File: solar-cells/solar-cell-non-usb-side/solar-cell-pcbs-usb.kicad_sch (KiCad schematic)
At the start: 13 parts, among them J1 Solar Cell

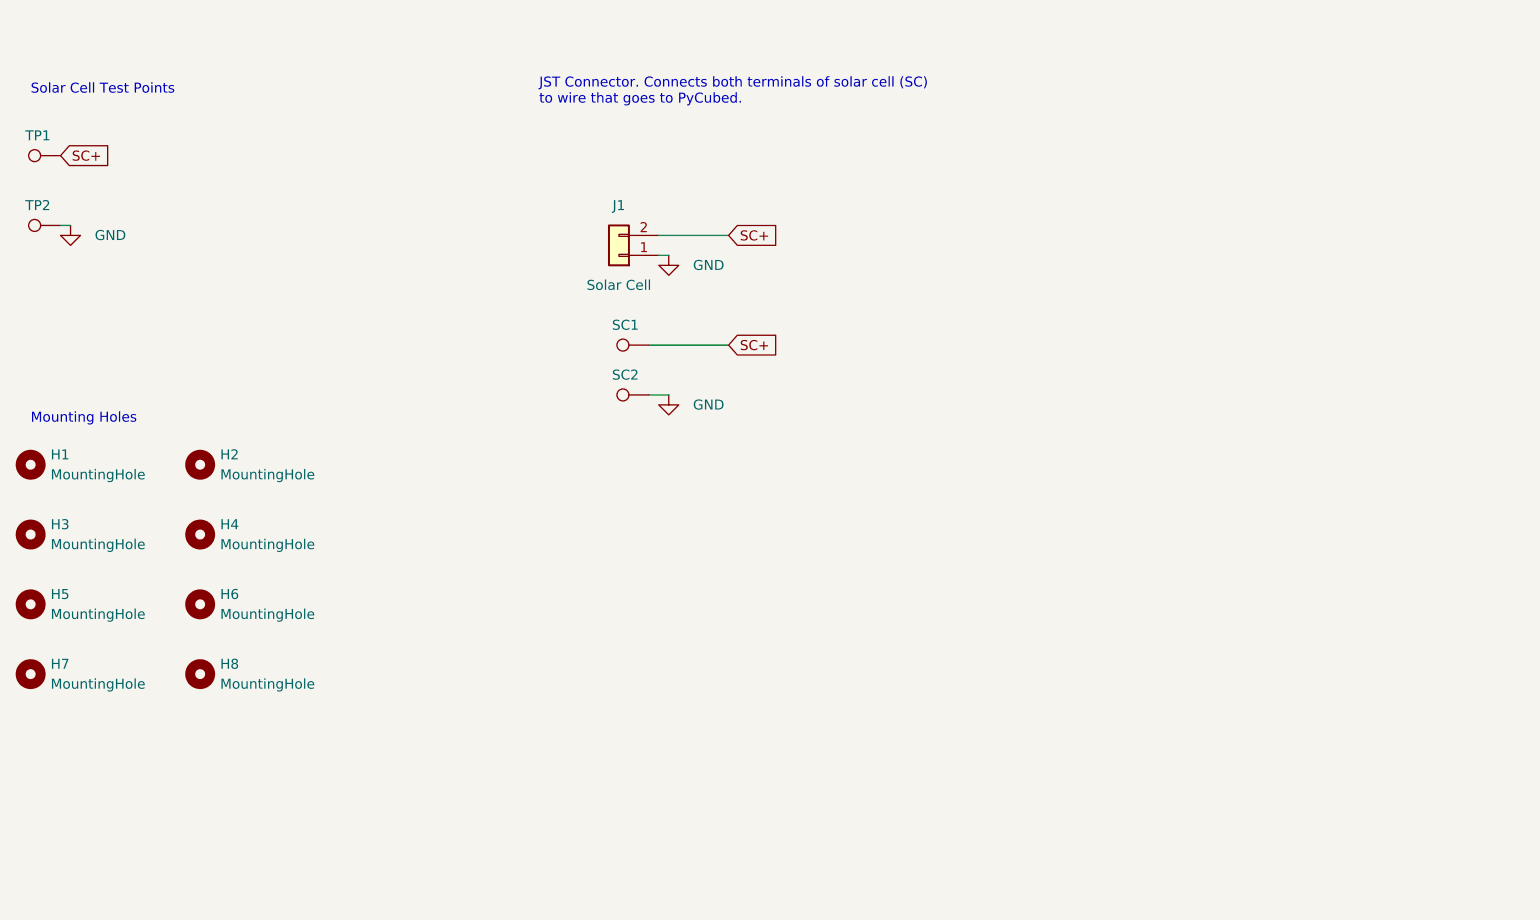
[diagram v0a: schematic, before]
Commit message: updated schematic for new solar cells
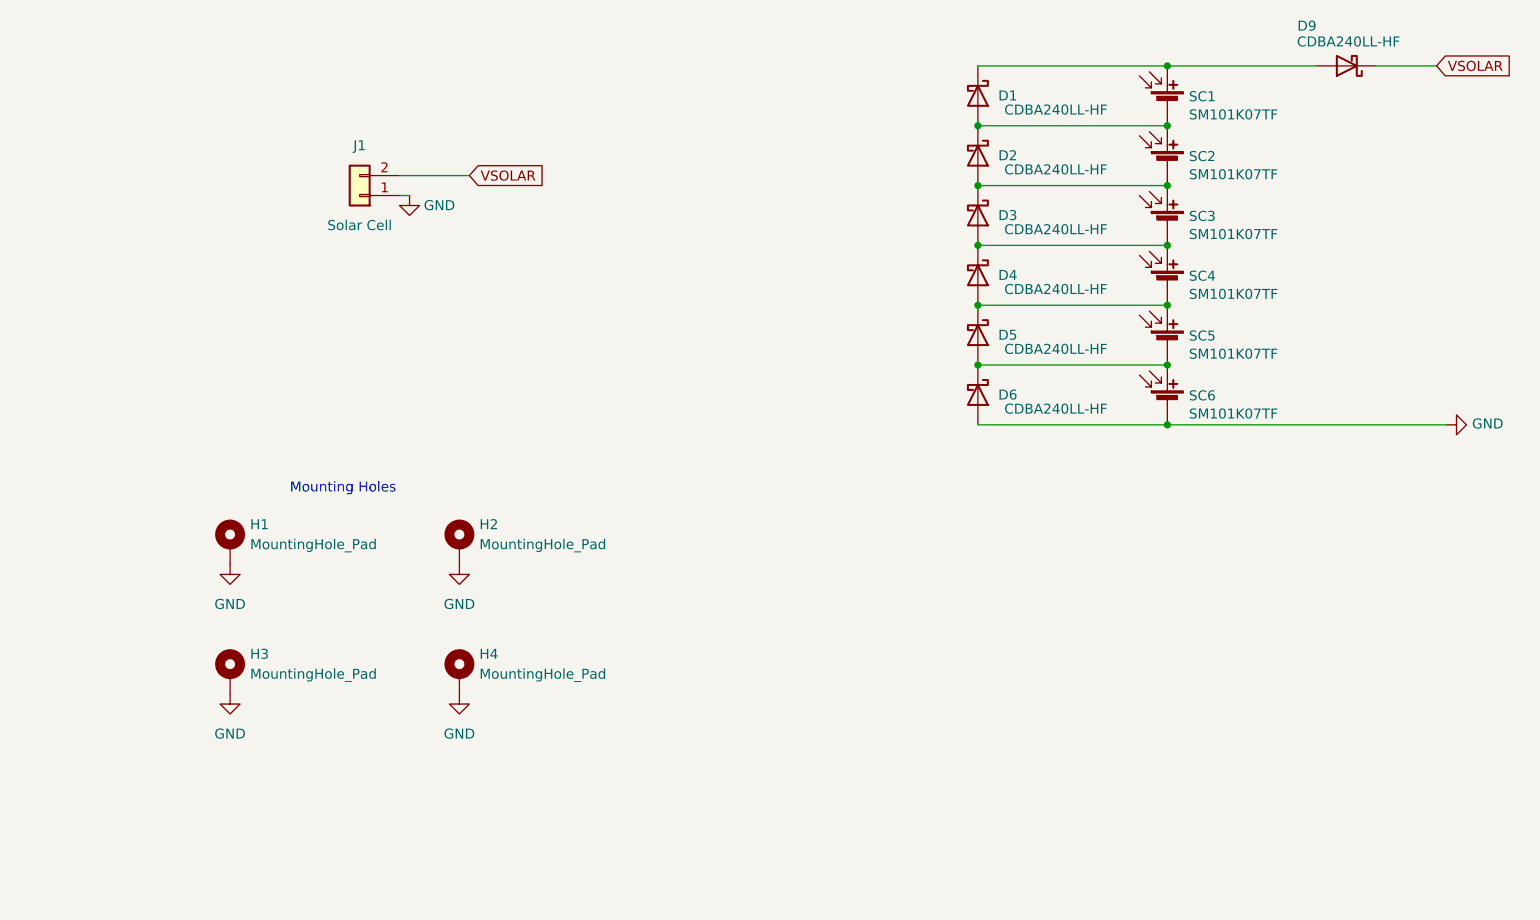
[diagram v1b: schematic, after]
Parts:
- removed H1, H2, H3, H4, H5, H6, H7, H8: MountingHole, MountingHole:MountingHole_3.2mm_M3_DIN965_Pad, symbol Mechanical:MountingHole
- removed SC1: SC+, TestPoint:TestPoint_THTPad_D3.0mm_Drill1.5mm, symbol Connector:TestPoint
- removed SC2: SC-, TestPoint:TestPoint_THTPad_D3.0mm_Drill1.5mm, symbol Connector:TestPoint
- removed TP1: SC+, TestPoint:TestPoint_Loop_D1.80mm_Drill1.0mm_Beaded, symbol Connector:TestPoint
- removed TP2: SC-, TestPoint:TestPoint_Loop_D1.80mm_Drill1.0mm_Beaded, symbol Connector:TestPoint
- added D1, D2, D3, D4, D5, D6, D9: CDBA240LL-HF, ISP:DO-214AC, symbol Device:D_Schottky
- added H1, H2, H3, H4: MountingHole_Pad, MountingHole:MountingHole_3.2mm_M3_DIN965_Pad, symbol Mechanical:MountingHole_Pad
- added SC1, SC2, SC3, SC4, SC5, SC6: SM101K07TF, ISP:SM101K07TF, symbol Device:Solar_Cell
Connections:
- net GND: now also D6.2 (A), H1.1, H2.1, H3.1, H4.1, SC6.2 (-)
- net SC+ renamed VSOLAR
- net VSOLAR: now also D9.1 (K)
- new net: D1.1 (K), D9.2 (A), SC1.1 (+)
- new net: D1.2 (A), D2.1 (K), SC1.2 (-), SC2.1 (+)
- new net: D4.2 (A), D5.1 (K), SC4.2 (-), SC5.1 (+)
- new net: D5.2 (A), D6.1 (K), SC5.2 (-), SC6.1 (+)
- new net: D2.2 (A), D3.1 (K), SC2.2 (-), SC3.1 (+)
- new net: D3.2 (A), D4.1 (K), SC3.2 (-), SC4.1 (+)
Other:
- note removed: "JST Connector. Connects both terminals of solar cell (SC) to wire that goes to PyCubed."
- note removed: "Solar Cell Test Points"
- title: Solar Cell PCBs  -> Solar Cell PCB - usb side

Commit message: hole positioning
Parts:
- added H5, H6, H7, H8: MountingHole_Pad, MountingHole:MountingHole_3.2mm_M3_DIN965_Pad, symbol Mechanical:MountingHole_Pad
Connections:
- net GND: now also H5.1, H6.1, H7.1, H8.1
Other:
- moved on the sheet: H1, H2, H3, H4
